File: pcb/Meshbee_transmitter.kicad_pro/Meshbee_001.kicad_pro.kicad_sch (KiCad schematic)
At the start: 24 parts, among them J1 sensor 0, J10 Battery, J11 ESP32, J2 sensor 1, J3 sensor 2, J4 sensor 3, J5 sensor 4, J6 sensor 5, J7 sensor 8, J8 sensor 9, J9 Reset_Button, SW1 button, SW2 reset, U1 Wemos_LoLin32_lite, U2 HT-RA62, U3 CD74HC4067M 16 channel multip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, U4 nice_nano

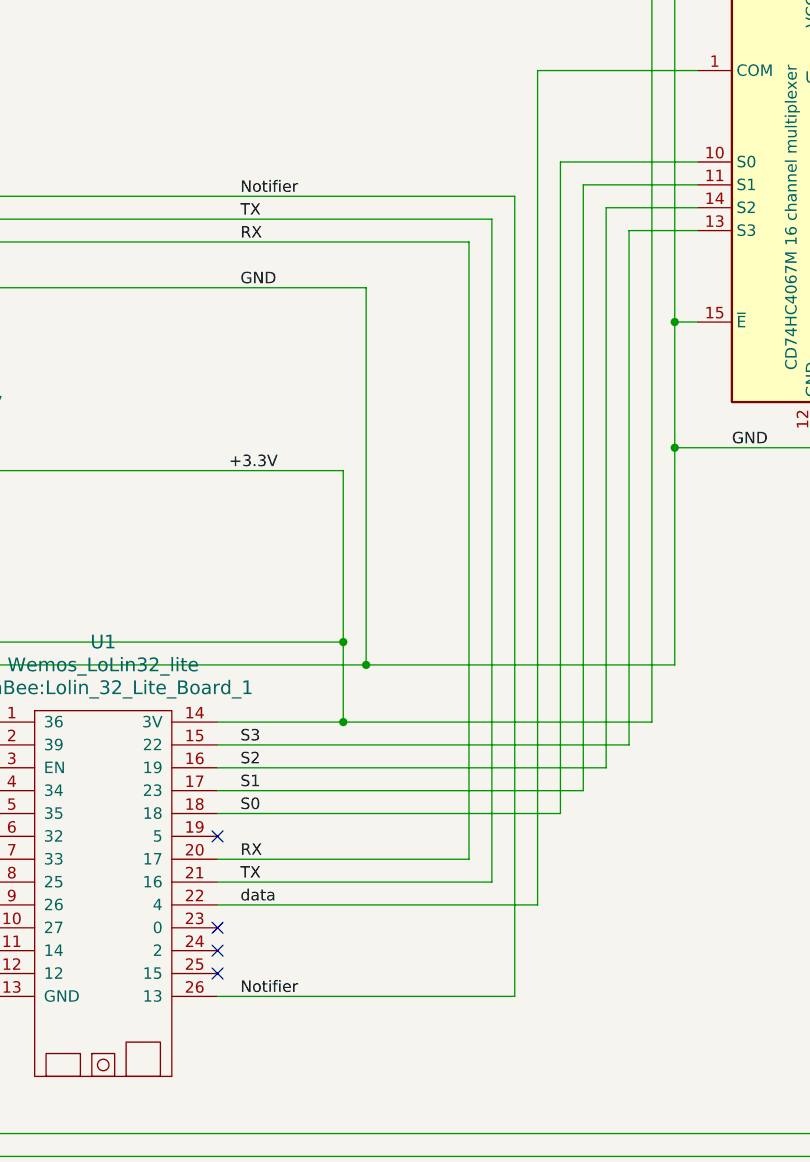
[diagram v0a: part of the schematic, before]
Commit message: - transferred some markings on the board to silkscreen layer - renumeration of WEMOS LOLIN32 LITE Pins - modified 3D-printed module for battery - created 3D-print module for MeshBee PCB
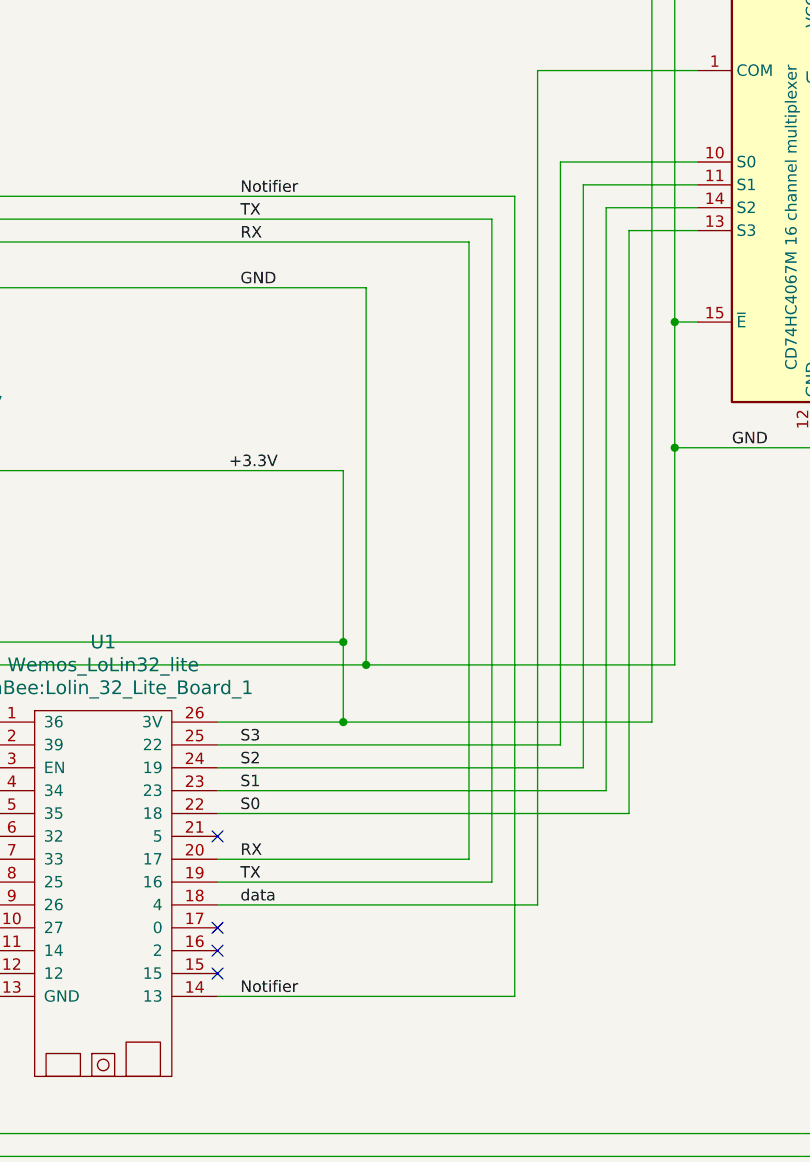
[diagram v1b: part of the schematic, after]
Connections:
- net +3.3V: now also U1.26 (3V); no longer U1.14 (3V)
- net Notifier: now also U1.14 (13); no longer U1.26 (13)
- net S0: now also U1.22 (18), U3.13 (S3); no longer U1.18, U3.10 (S0)
- net S1: now also U1.23, U3.14 (S2); no longer U1.17 (23), U3.11 (S1)
- net S2: now also U1.24 (19), U3.11 (S1); no longer U1.16 (19), U3.14 (S2)
- net S3: now also U1.25 (22), U3.10 (S0); no longer U1.15 (22), U3.13 (S3)
- net TX: now also U1.19 (16); no longer U1.21 (16)
- net data: now also U1.18 (4); no longer U1.22 (4)
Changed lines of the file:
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@@
 	(wire
 		(pts
-			(xy 234.95 146.05) (xy 234.95 203.2)
+			(xy 234.95 146.05) (xy 234.95 210.82)
 		)
 		(stroke
@@
 	(wire
 		(pts
-			(xy 227.33 138.43) (xy 227.33 210.82)
+			(xy 227.33 138.43) (xy 227.33 203.2)
 		)
 		(stroke
@@
 	(wire
 		(pts
-			(xy 227.33 210.82) (xy 189.23 210.82)
-		)
-		(stroke
-			(width 0)
-			(type default)
-		)
-	)
-	(wire
-		(pts
 			(xy 148.59 194.31) (xy 148.59 231.14)
 		)
@@
 	(wire
 		(pts
+			(xy 189.23 205.74) (xy 229.87 205.74)
+		)
+		(stroke
+			(width 0)
+			(type default)
+		)
+	)
+	(wire
+		(pts
 			(xy 162.56 152.4) (xy 162.56 154.94)
 		)
@@
 	(wire
 		(pts
+			(xy 189.23 203.2) (xy 227.33 203.2)
+		)
+		(stroke
+			(width 0)
+			(type default)
+		)
+	)
+	(wire
+		(pts
 			(xy 337.82 140.97) (xy 337.82 149.86)
 		)
@@
 	(wire
 		(pts
-			(xy 229.87 208.28) (xy 189.23 208.28)
-		)
-		(stroke
-			(width 0)
-			(type default)
-		)
-	)
-	(wire
-		(pts
 			(xy 124.46 161.29) (xy 129.54 161.29)
 		)
@@
 	(wire
 		(pts
+			(xy 189.23 210.82) (xy 234.95 210.82)
+		)
+		(stroke
+			(width 0)
+			(type default)
+		)
+	)
+	(wire
+		(pts
 			(xy 267.97 123.19) (xy 271.78 123.19)
 		)
@@
 	(wire
 		(pts
-			(xy 229.87 140.97) (xy 229.87 208.28)
+			(xy 229.87 140.97) (xy 229.87 205.74)
 		)
 		(stroke
@@
 	(wire
 		(pts
-			(xy 234.95 203.2) (xy 189.23 203.2)
-		)
-		(stroke
-			(width 0)
-			(type default)
-		)
-	)
-	(wire
-		(pts
 			(xy 27.94 147.32) (xy 73.66 147.32)
 		)
@@
 	(wire
 		(pts
+			(xy 189.23 208.28) (xy 232.41 208.28)
+		)
+		(stroke
+			(width 0)
+			(type default)
+		)
+	)
+	(wire
+		(pts
 			(xy 153.67 240.03) (xy 153.67 246.38)
 		)
@@
 	(wire
 		(pts
-			(xy 232.41 205.74) (xy 189.23 205.74)
-		)
-		(stroke
-			(width 0)
-			(type default)
-		)
-	)
-	(wire
-		(pts
 			(xy 332.74 149.86) (xy 332.74 162.56)
 		)
@@
 	(wire
 		(pts
-			(xy 232.41 143.51) (xy 232.41 205.74)
-		)
-		(stroke
+			(xy 232.41 143.51) (xy 232.41 208.28)
+		)
+		(stroke

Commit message: - added possibility to measure battery voltage with the ESP32 to transmit to database
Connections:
- net at U1.6 (32): now also R3.1, R4.2, U4.21 (D21/P0.31)
- no-connect marks 22 -> 21
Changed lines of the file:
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@@
+	)
+	(junction
+		(at 121.92 222.25)
+		(diameter 0)
+		(color 0 0 0 0)
 	)
 	(junction
@@
 		(diameter 0)
 		(color 0 0 0 0)
-	)
-	(no_connect
-		(at 163.83 213.36)
 	)
 	(no_connect
@@
 	(wire
 		(pts
+			(xy 143.51 213.36) (xy 163.83 213.36)
+		)
+		(stroke
+			(width 0)
+			(type default)
+		)
+	)
+	(wire
+		(pts
 			(xy 314.96 153.67) (xy 314.96 162.56)
 		)
@@
 	(wire
 		(pts
+			(xy 143.51 222.25) (xy 143.51 213.36)
+		)
+		(stroke
+			(width 0)
+			(type default)
+		)
+	)
+	(wire
+		(pts
 			(xy 38.1 154.94) (xy 38.1 157.48)
 		)
@@
 		)
 		(stroke
+			(width 0)
+			(type default)
+		)
+	)
+	(wire
+		(pts
+			(xy 121.92 222.25) (xy 143.51 222.25)
+		)
+		(stroke

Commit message: - changed load cell holder design - changed some labels in the circuit
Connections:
- net S0: now also U1.25 (22), U3.10 (S0); no longer U1.22 (18), U3.13 (S3)
- net S1: now also U1.24 (19), U3.11 (S1); no longer U1.23, U3.14 (S2)
- net S2: now also U1.23, U3.14 (S2); no longer U1.24 (19), U3.11 (S1)
- net S3: now also U1.22 (18), U3.13 (S3); no longer U1.25 (22), U3.10 (S0)
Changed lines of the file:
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@@
 		)
 	)
-	(label "S2"
+	(label "S1"
 		(at 191.77 205.74 0)
 		(effects
@@
 		)
 	)
-	(label "S3"
+	(label "S0"
 		(at 191.77 203.2 0)
 		(effects
@@
 		)
 	)
-	(label "S0"
+	(label "S3"
 		(at 191.77 210.82 0)
 		(effects
@@
 		)
 	)
-	(label "S1"
+	(label "S2"
 		(at 191.77 208.28 0)
 		(effects

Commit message: - added capacitor on NRF52480 power lines, for possible crashes of nrf52840 during switch from solar panel to battery due to power glitches - changed GPIO of S3 pin of multiplexer to use GPIO22  for internal led as status indicator
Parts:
- added C1: 100nF, Capacitor_THT:CP_Radial_Tantal_D5.0mm_P2.50mm, symbol Device:C_Polarized
- added C2: 47µF, Capacitor_THT:CP_Radial_D5.0mm_P2.00mm, symbol Device:C_Polarized
- J7: value sensor 8 -> sensor 6
- J8: value sensor 9 -> sensor 7
- J9: value Reset_Button -> Reset/AP_Button
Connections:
- net +3.3V: now also C1.1, C2.1
- net GND: now also C1.2, C2.2
- net S3: now also U1.10 (27); no longer U1.22 (18)
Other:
- moved on the sheet: SW1, SW2
